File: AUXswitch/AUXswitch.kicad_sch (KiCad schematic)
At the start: 25 parts, among them J1 Conn_02x04_Counter_Clockwise, J10 5V_IN, J2 Conn_01x03, J3 INPUT_1, J4 INPUT_2, J5 OUTPUT, J6 LIVE_IN, J7 LIVE_OUT, J9 LIVE_OUT_SMP, K1 HRS2H-S-DC5V-N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

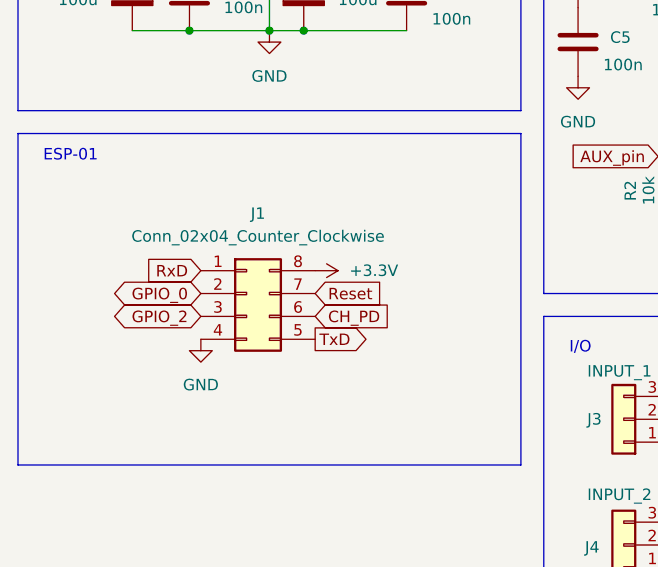
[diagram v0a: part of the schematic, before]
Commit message: fixede pinouts
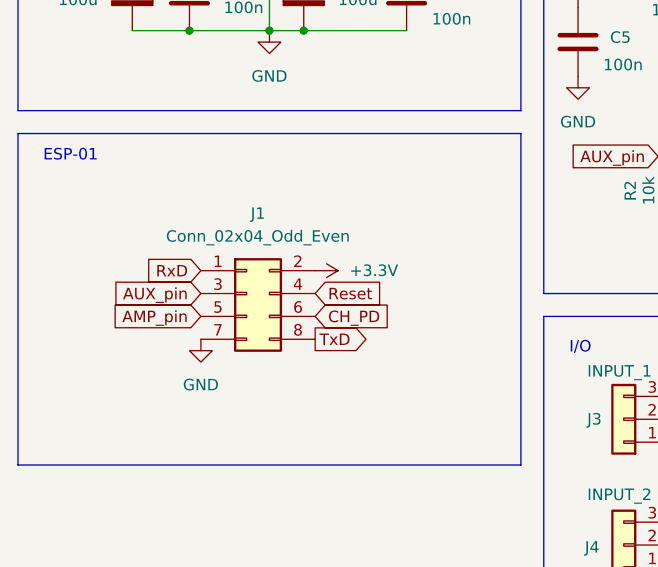
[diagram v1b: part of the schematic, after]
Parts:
- removed J1: Conn_02x04_Counter_Clockwise, Connector_PinSocket_2.54mm:PinSocket_2x04_P2.54mm_Vertical, symbol Connector_Generic:Conn_02x04_Counter_Clockwise
- added J1: Conn_02x04_Odd_Even, Connector_PinHeader_2.54mm:PinHeader_2x04_P2.54mm_Vertical, symbol Connector_Generic:Conn_02x04_Odd_Even
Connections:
- net +3.3V: now also J1.2 (Pin_2)
- net AMP_pin: now also J1.5 (Pin_5)
- net AUX_pin: now also J1.3 (Pin_3)
- net CH_PD: now also J1.6 (Pin_6)
- net GND: now also J1.7 (Pin_7)
- net Reset: now also J1.4 (Pin_4)
- net RxD: now also J1.1 (Pin_1)
- net TxD: now also J1.8 (Pin_8)
